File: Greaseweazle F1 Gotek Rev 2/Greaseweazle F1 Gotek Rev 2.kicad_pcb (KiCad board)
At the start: 2 copper layers, 111.6 x 94.4 mm, 56 parts, among them CN1 Floppy Data, J1 PinHeader_1x04_P2.54mm_Vertic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, J1 SWD, J2 Floppy Power, J2 PinHeader_1x04_P2.54mm_Vertic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, J3 PinHeader_1x04_P2.54mm_Vertic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, J3 Programming Port, J4 USB B, J5 Boot Header, J6 LEDC68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

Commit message: Latest updates to GW F1 Gotek Rev 2 and GW F1 3.5 rev 2
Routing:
- net GND: vias 28 -> 60
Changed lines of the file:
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@@
     (thickness 1.6)
     (drawings 335)
-    (tracks 573)
+    (tracks 605)
     (zones 0)
     (modules 56)
@@
   (via (at 162.6743 110.7694) (size 0.6) (drill 0.4) (layers F.Cu B.Cu) (net 1))
   (via (at 159.9946 109.2581) (size 0.6) (drill 0.4) (layers F.Cu B.Cu) (net 1))
+  (via (at 106.68 76.2) (size 0.6) (drill 0.4) (layers F.Cu B.Cu) (net 1))
+  (via (at 119.38 76.2) (size 0.6) (drill 0.4) (layers F.Cu B.Cu) (net 1))
+  (via (at 111.76 68.58) (size 0.6) (drill 0.4) (layers F.Cu B.Cu) (net 1))
+  (via (at 121.92 68.58) (size 0.6) (drill 0.4) (layers F.Cu B.Cu) (net 1))
+  (via (at 111.76 60.96) (size 0.6) (drill 0.4) (layers F.Cu B.Cu) (net 1))
+  (via (at 116.84 50.8) (size 0.6) (drill 0.4) (layers F.Cu B.Cu) (net 1))
+  (via (at 127 50.8) (size 0.6) (drill 0.4) (layers F.Cu B.Cu) (net 1))
+  (via (at 137.16 50.8) (size 0.6) (drill 0.4) (layers F.Cu B.Cu) (net 1))
+  (via (at 175.26 48.26) (size 0.6) (drill 0.4) (layers F.Cu B.Cu) (net 1))
+  (via (at 177.8 60.96) (size 0.6) (drill 0.4) (layers F.Cu B.Cu) (net 1))
+  (via (at 195.58 73.66) (size 0.6) (drill 0.4) (layers F.Cu B.Cu) (net 1))
+  (via (at 172.72 104.14) (size 0.6) (drill 0.4) (layers F.Cu B.Cu) (net 1))
+  (via (at 190.5 124.46) (size 0.6) (drill 0.4) (layers F.Cu B.Cu) (net 1))
+  (via (at 190.5 116.84) (size 0.6) (drill 0.4) (layers F.Cu B.Cu) (net 1))
+  (via (at 177.8 119.38) (size 0.6) (drill 0.4) (layers F.Cu B.Cu) (net 1))
+  (via (at 154.94 121.92) (size 0.6) (drill 0.4) (layers F.Cu B.Cu) (net 1))
+  (via (at 144.78 124.46) (size 0.6) (drill 0.4) (layers F.Cu B.Cu) (net 1))
+  (via (at 144.78 116.84) (size 0.6) (drill 0.4) (layers F.Cu B.Cu) (net 1))
+  (via (at 124.46 129.54) (size 0.6) (drill 0.4) (layers F.Cu B.Cu) (net 1))
+  (via (at 116.84 129.54) (size 0.6) (drill 0.4) (layers F.Cu B.Cu) (net 1))
+  (via (at 96.52 124.46) (size 0.6) (drill 0.4) (layers F.Cu B.Cu) (net 1))
+  (via (at 124.46 104.14) (size 0.6) (drill 0.4) (layers F.Cu B.Cu) (net 1))
+  (via (at 109.22 91.44) (size 0.6) (drill 0.4) (layers F.Cu B.Cu) (net 1))
+  (via (at 172.72 60.96) (size 0.6) (drill 0.4) (layers F.Cu B.Cu) (net 1))
+  (via (at 193.04 68.58) (size 0.6) (drill 0.4) (layers F.Cu B.Cu) (net 1))
+  (via (at 167.64 106.68) (size 0.6) (drill 0.4) (layers F.Cu B.Cu) (net 1))
+  (via (at 162.56 104.14) (size 0.6) (drill 0.4) (layers F.Cu B.Cu) (net 1))
+  (via (at 142.24 83.82) (size 0.6) (drill 0.4) (layers F.Cu B.Cu) (net 1))
+  (via (at 134.62 83.82) (size 0.6) (drill 0.4) (layers F.Cu B.Cu) (net 1))
+  (via (at 193.04 101.6) (size 0.6) (drill 0.4) (layers F.Cu B.Cu) (net 1))
+  (via (at 180.34 109.22) (size 0.6) (drill 0.4) (layers F.Cu B.Cu) (net 1))
+  (via (at 137.16 116.84) (size 0.6) (drill 0.4) (layers F.Cu B.Cu) (net 1))
   (segment (start 186.1058 74.6887) (end 186.1058 71.7527) (width 0.5) (layer F.Cu) (net 2))
   (segment (start 189.2554 74.6252) (end 189.2554 71.7527) (width 0.5) (layer F.Cu) (net 2))

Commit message: Corrected 12V LED resistor from 2K to 4.7K
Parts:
- R11: value 2K -> 4.7K
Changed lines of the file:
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@@
       (effects (font (size 1 1) (thickness 0.15)))
     )
-    (fp_text value 2K (at 0 1.65) (layer F.SilkS)
+    (fp_text value 4.7K (at 0 1.65) (layer F.SilkS)
       (effects (font (size 1 1) (thickness 0.15)))
     )

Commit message: Added DWGS.User layer
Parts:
- added REF**: Floppy_Drive, solarmon_library:Floppy_Drive, F.Cu at (154.2, 85.9)

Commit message: Added warning about PCB thickness, and grounded USB shield
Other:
- board text added: "Important: PCB thickness should be 1mm!"
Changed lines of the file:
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@@
   (general
     (thickness 1.6)
-    (drawings 335)
+    (drawings 336)
     (tracks 605)
     (zones 0)
@@
     (uvia_drill 0.1)
   )
+  (module w_conn_pc:conn_usb_B (layer F.Cu)
+    (at 95.504 124.5 270)
+    (descr "USB B-type receptacle, Lumberg P/N 2411-02")
+    (tags USB)
+    (fp_text reference J4 (at -6.5278 -10.0076 180) (layer F.SilkS)
+      (effects (font (size 1.524 1.524) (thickness 0.3048)))
+    )
+    (fp_text value "USB B" (at -0.1778 -9.7282 270) (layer F.SilkS)
+      (effects (font (size 1.524 1.524) (thickness 0.3048)))
+    )
+    (fp_line (start -6.0198 -8.001) (end -6.0198 -2.286) (layer F.SilkS) (width 0.254))
+    (fp_line (start 6.0198 -8.001) (end -6.0198 -8.001) (layer F.SilkS) (width 0.254))
+    (fp_line (start 6.0198 -2.286) (end 6.0198 -8.001) (layer F.SilkS) (width 0.254))
+    (fp_line (start 6.0198 8.0264) (end 6.0198 -2.286) (layer F.SilkS) (width 0.254))
+    (fp_line (start -6.0198 8.0264) (end 6.0198 8.0264) (layer F.SilkS) (width 0.254))
+    (fp_line (start -6.0198 -2.286) (end -6.0198 8.0264) (layer F.SilkS) (width 0.254))
+    (fp_line (start -7.7724 -2.286) (end -6.0198 -0.5334) (layer F.SilkS) (width 0.254))
+    (fp_line (start -6.0198 -4.0386) (end -7.7724 -2.286) (layer F.SilkS) (width 0.254))
+    (fp_line (start 7.7724 -2.286) (end 6.0198 -0.5334) (layer F.SilkS) (width 0.254))
+    (fp_line (start 6.0198 -4.0386) (end 7.7724 -2.286) (layer F.SilkS) (width 0.254))
+    (pad 5 thru_hole circle (at 6.0198 -2.286 270) (size 3.50012 3.50012) (drill 2.30124) (layers *.Cu *.Mask)
+      (net 1 GND))
+    (pad 5 thru_hole circle (at -6.0198 -2.286 270) (size 3.50012 3.50012) (drill 2.30124) (layers *.Cu *.Mask)
+      (net 1 GND))
+    (pad 2 thru_hole circle (at -1.2446 -7.0104 270) (size 1.50114 1.50114) (drill 0.94996) (layers *.Cu *.Mask)
+      (net 48 "Net-(J4-Pad2)"))
+    (pad 1 thru_hole circle (at 1.2446 -7.0104 270) (size 1.50114 1.50114) (drill 0.94996) (layers *.Cu *.Mask)
+      (net 3 +5V))
+    (pad 4 thru_hole circle (at 1.2446 -5.0038 270) (size 1.50114 1.50114) (drill 0.94996) (layers *.Cu *.Mask)
+      (net 1 GND))
+    (pad 3 thru_hole circle (at -1.2446 -5.0038 270) (size 1.50114 1.50114) (drill 0.94996) (layers *.Cu *.Mask)
+      (net 49 "Net-(J4-Pad3)"))
+    (model "${KISYS3DMOD}/usb-b/USB 2.0 Type B Connector Right Angle (Würth 61400416121).step"
+      (offset (xyz 1.3 7 0))
+      (scale (xyz 1 1 1))
+      (rotate (xyz 0 0 0))
+    )
+  )
   (module solarmon_library:Floppy_Drive (layer F.Cu)
     (at 154.2288 85.9282)
@@
     )
   )
-  (module w_conn_pc:conn_usb_B (layer F.Cu)
-    (at 95.504 124.5 270)
-    (descr "USB B-type receptacle, Lumberg P/N 2411-02")
-    (tags USB)
-    (fp_text reference J4 (at -6.5278 -10.0076 180) (layer F.SilkS)
-      (effects (font (size 1.524 1.524) (thickness 0.3048)))
-    )
-    (fp_text value "USB B" (at -0.1778 -9.7282 90) (layer F.SilkS)
-      (effects (font (size 1.524 1.524) (thickness 0.3048)))
-    )
-    (fp_line (start -6.0198 -8.001) (end -6.0198 -2.286) (layer F.SilkS) (width 0.254))
-    (fp_line (start 6.0198 -8.001) (end -6.0198 -8.001) (layer F.SilkS) (width 0.254))
-    (fp_line (start 6.0198 -2.286) (end 6.0198 -8.001) (layer F.SilkS) (width 0.254))
-    (fp_line (start 6.0198 8.0264) (end 6.0198 -2.286) (layer F.SilkS) (width 0.254))
-    (fp_line (start -6.0198 8.0264) (end 6.0198 8.0264) (layer F.SilkS) (width 0.254))
-    (fp_line (start -6.0198 -2.286) (end -6.0198 8.0264) (layer F.SilkS) (width 0.254))
-    (fp_line (start -7.7724 -2.286) (end -6.0198 -0.5334) (layer F.SilkS) (width 0.254))
-    (fp_line (start -6.0198 -4.0386) (end -7.7724 -2.286) (layer F.SilkS) (width 0.254))
-    (fp_line (start 7.7724 -2.286) (end 6.0198 -0.5334) (layer F.SilkS) (width 0.254))
-    (fp_line (start 6.0198 -4.0386) (end 7.7724 -2.286) (layer F.SilkS) (width 0.254))
-    (pad "" thru_hole circle (at 6.0198 -2.286 270) (size 3.50012 3.50012) (drill 2.30124) (layers *.Cu *.Mask))
-    (pad "" thru_hole circle (at -6.0198 -2.286 270) (size 3.50012 3.50012) (drill 2.30124) (layers *.Cu *.Mask))
-    (pad 2 thru_hole circle (at -1.2446 -7.0104 270) (size 1.50114 1.50114) (drill 0.94996) (layers *.Cu *.Mask)
-      (net 48 "Net-(J4-Pad2)"))
-    (pad 1 thru_hole circle (at 1.2446 -7.0104 270) (size 1.50114 1.50114) (drill 0.94996) (layers *.Cu *.Mask)
-      (net 3 +5V))
-    (pad 4 thru_hole circle (at 1.2446 -5.0038 270) (size 1.50114 1.50114) (drill 0.94996) (layers *.Cu *.Mask)
-      (net 1 GND))
-    (pad 3 thru_hole circle (at -1.2446 -5.0038 270) (size 1.50114 1.50114) (drill 0.94996) (layers *.Cu *.Mask)
-      (net 49 "Net-(J4-Pad3)"))
-    (model "${KISYS3DMOD}/usb-b/USB 2.0 Type B Connector Right Angle (Würth 61400416121).step"
-      (offset (xyz 1.3 7 0))
-      (scale (xyz 1 1 1))
-      (rotate (xyz 0 0 0))
-    )
-  )
   (module Connector_PinHeader_2.54mm:PinHeader_1x04_P2.54mm_Horizontal (layer F.Cu)
     (at 198.12 81.3308)
@@
       (net 1 GND) (zone_connect 2))
   )
+  (gr_text "Important: PCB thickness should be 1mm!" (at 119.761 48.895) (layer F.SilkS)
+    (effects (font (size 1.3 1.3) (thickness 0.15)) (justify left))
+  )
   (gr_line (start 107.823 111.506) (end 107.823 111.633) (layer F.SilkS) (width 0.12))

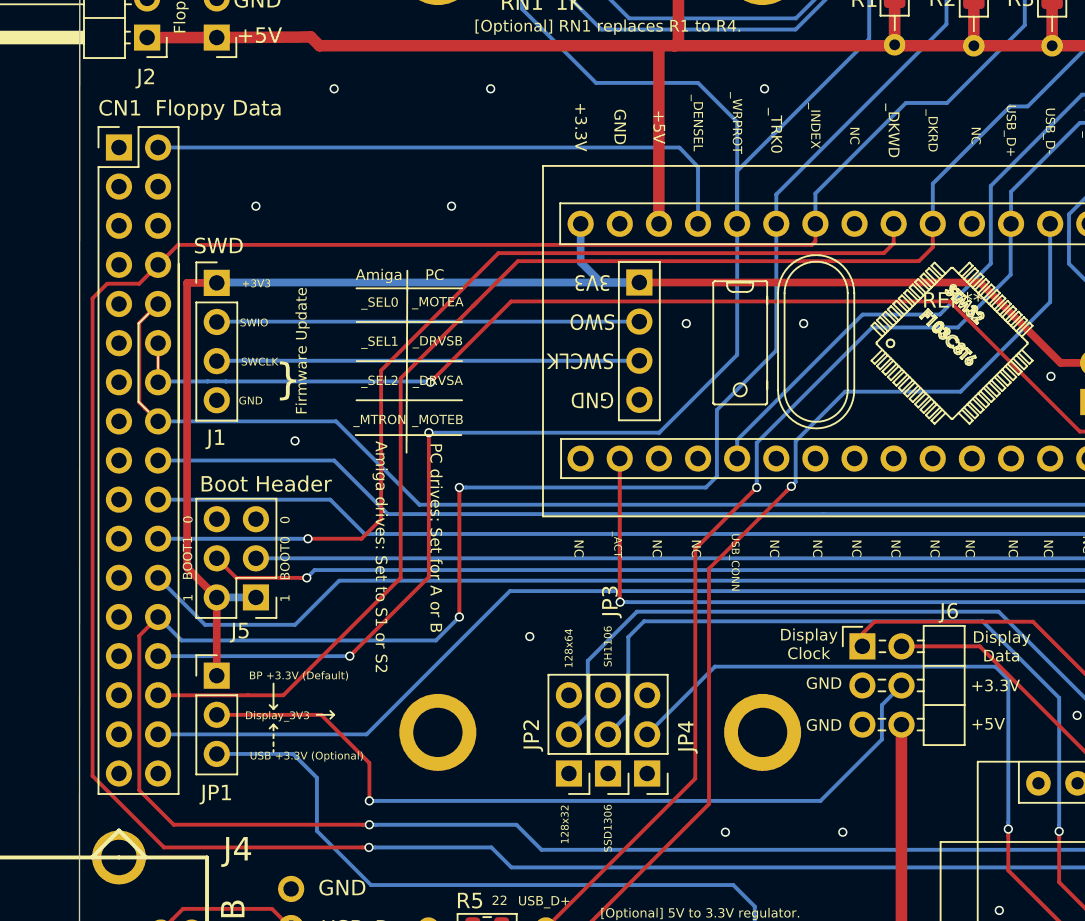
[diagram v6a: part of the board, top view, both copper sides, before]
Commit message: Added missing pin 1 and 34 silkscreen for floppy data connector
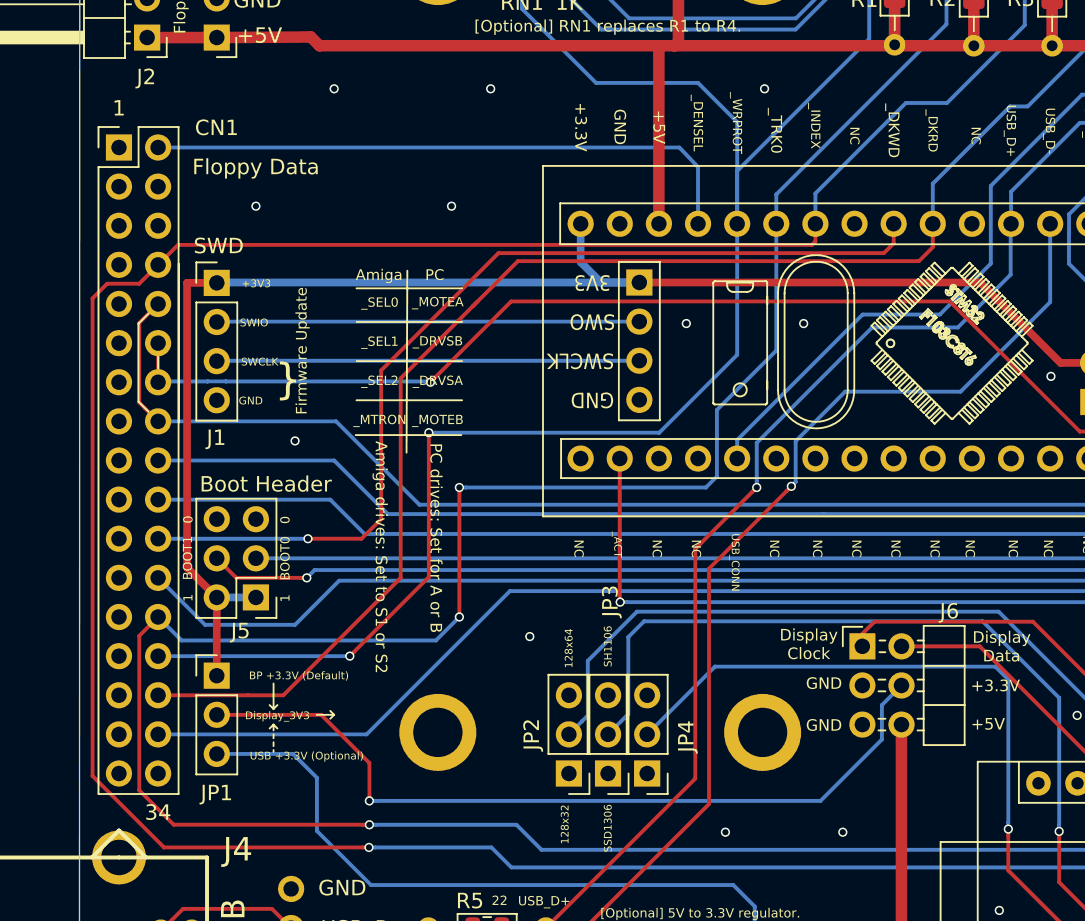
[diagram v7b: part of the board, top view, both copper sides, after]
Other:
- board text added: "34"
